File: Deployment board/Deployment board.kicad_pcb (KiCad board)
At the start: 2 copper layers, 50 x 50 mm, 27 parts, among them J1 Conn_01x04, J2 Conn_01x04, J3 Conn_01x02, J4 Conn_01x02, J5 Conn_01x02, M1 Motor_Servo, Q1 IRLR7843, Q2 IRLR7843, Q3 To be determined

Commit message: some changes on Deployment board pcb
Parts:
- C2: footprint Capacitor_THT:C_Radial_D10.0mm_H20.0mm_P5.00mm -> Capacitor_THT:C_Radial_D8.0mm_H7.0mm_P3.50mm
- moved D3 119.5 mm to (33.3, 150.1)
- moved R4 118.8 mm to (32.8, 147.1)
- moved GND1 118.7 mm to (37.0, 147.0)
- moved J3 113.1 mm to (27.4, 147.7)
- moved D6 108.6 mm to (39.0, 150.0)
- moved Q1 106.3 mm to (36.8, 141.6)
- moved V_D_BAT+1 105.9 mm to (39.5, 147.0)
- moved R7 105.7 mm to (43.2, 149.4), turned to 90 degrees
- moved R1 101.2 mm to (42.0, 136.0)
- moved D1 93.3 mm to (32.5, 136.0), turned to 180 degrees
- moved J1 92.7 mm to (27.4, 135.7)
- moved R6 90.0 mm to (37.0, 118.0)
- moved D5 81.1 mm to (42.5, 127.0), turned to 90 degrees
- moved R3 81.0 mm to (36.5, 136.0)
- moved F1 80.5 mm to (40.0, 119.0), turned to -90 degrees
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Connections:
- J3 pad 1: Net-(D3-A) -> V_Ｄ_BAT+
- J3 pad 2: unconnected-(J3-Pin_2-Pad2) -> Net-(D3-A)
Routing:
- net GND: track 0.00 -> 142.0 mm
- net V_Ｄ_BAT+: track 0.00 -> 52.8 mm
- net Net-(D3-A): track 0.00 -> 21.2 mm
- net Net-(D1-K): track 0.00 -> 19.3 mm
- net Main_AV_FIRE: track 0.00 -> 18.9 mm
- net Net-(D4-A): track 0.00 -> 16.0 mm
- net Backup_AV_FIRE: track 0.00 -> 13.1 mm
- net Backup_AV_PWM_Servo: track 0.00 -> 9.96 mm
- net Net-(D5-A2): track 0.00 -> 7.00 mm
- net V_D_BAT+: track 0.00 -> 4.25 mm
- net Main_AV_PWM_Servo: track 0.00 -> 4.22 mm
- net Net-(Q3-G): track 0.00 -> 3.49 mm
- net Net-(J5-Pin_1): track 0.00 -> 3.27 mm
- net Net-(D3-K): track 0.00 -> 3.01 mm
- net Net-(D6-A): track 0.00 -> 2.85 mm
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- added copper zone on B.Cu, net GND
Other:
- board size 50 x 50 mm -> 29.5 x 46.5 mm

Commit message: update Deployment board
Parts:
- J5: footprint Connector_PinHeader_2.54mm:PinHeader_1x02_P2.54mm_Vertical -> Connector_PinHeader_2.54mm:PinHeader_1x02_P2.54mm_Horizontal
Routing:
- net GND: track 142.0 -> 143.7 mm
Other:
- board size 29.5 x 46.5 mm -> 35.5 x 46.5 mm

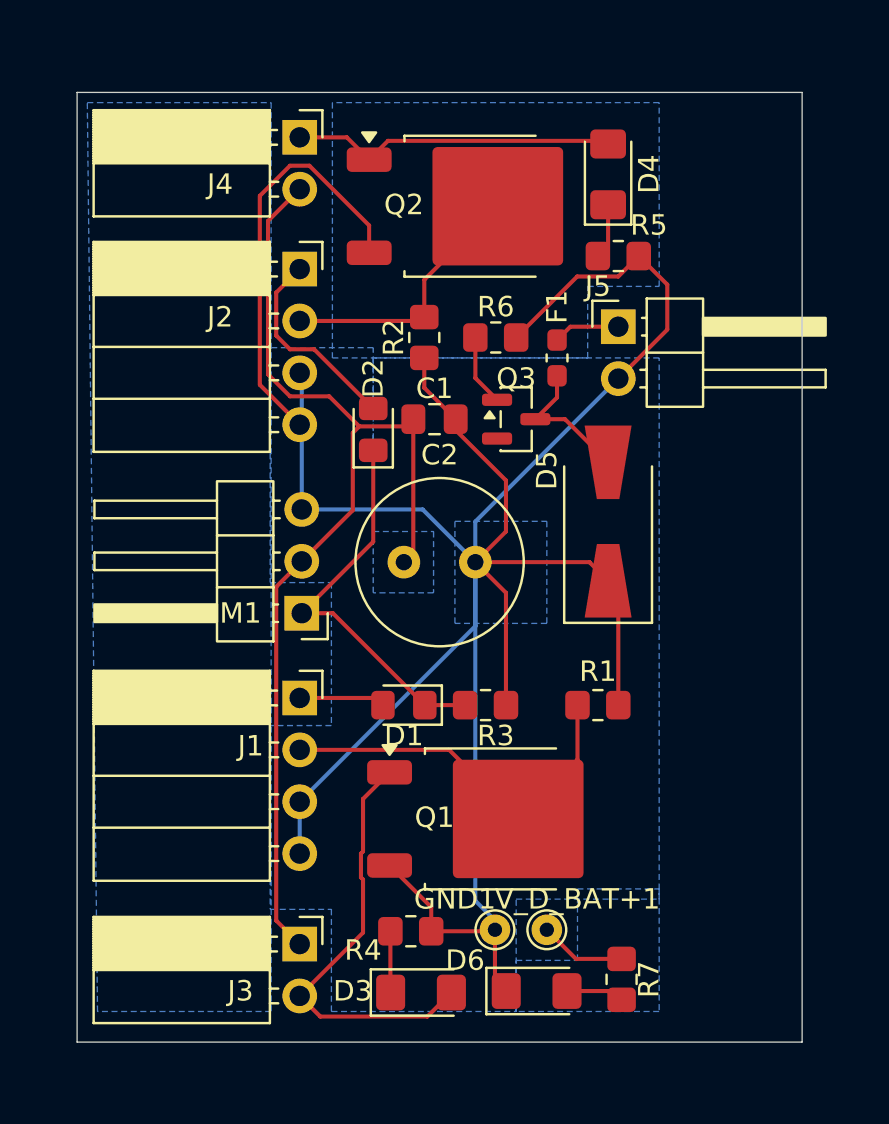
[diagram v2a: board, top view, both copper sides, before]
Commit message: add hole to connect wire
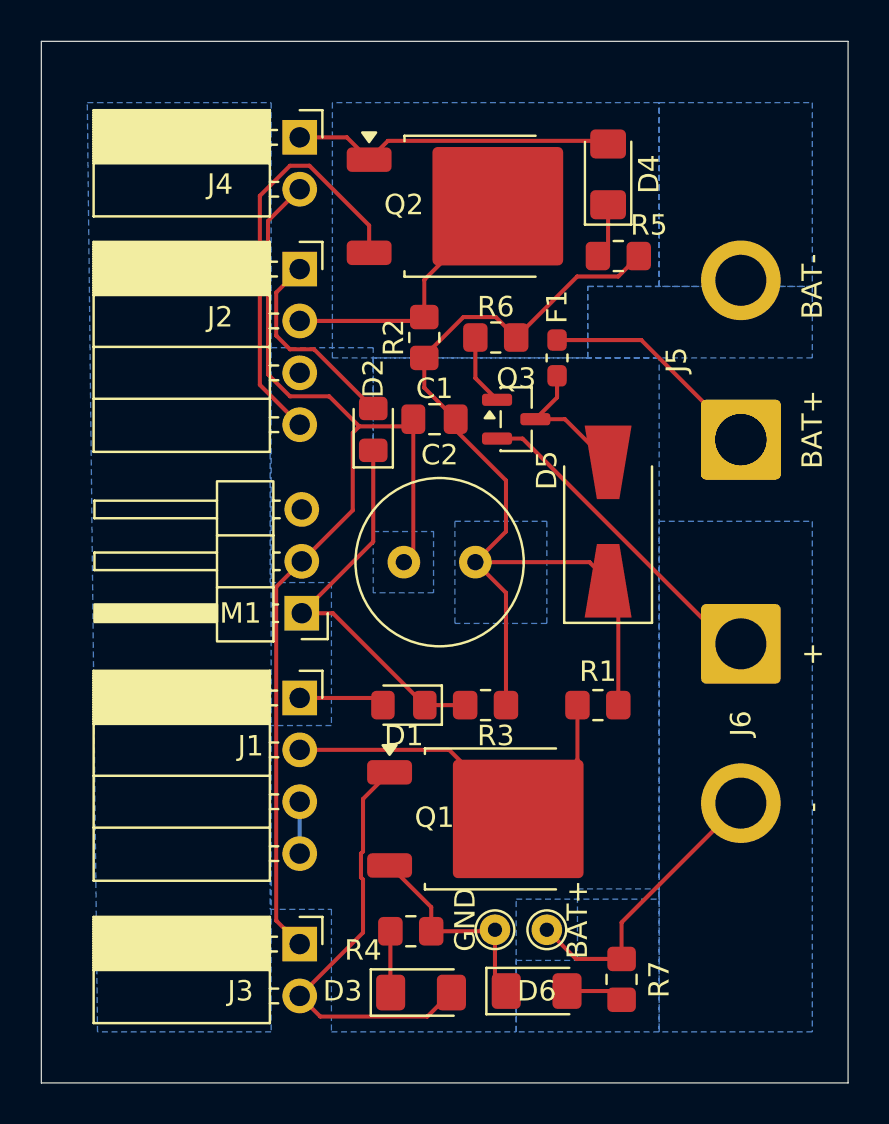
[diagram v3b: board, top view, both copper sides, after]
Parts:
- added ?: , , F.Cu at (49.0, 123.0)
- added J6: REMOVE BEFORE FLIGHT, Connector_Wire:SolderWire-2sqmm_1x02_P7.8mm_D2mm_OD3.9mm, F.Cu at (49.0, 133.0)
- J5: footprint Connector_PinHeader_2.54mm:PinHeader_1x02_P2.54mm_Horizontal -> Connector_Wire:SolderWire-2sqmm_1x02_P7.8mm_D2mm_OD3.9mm
- moved J5 8.16 mm to (49.0, 123.0), turned to 90 degrees
- renumbered V_D_BAT+1 to BAT+, GND1 to GND
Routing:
- net GND: track 143.7 -> 80.6 mm
- net Net-(J6-A): track 0.00 -> 16.1 mm
- net V_D_BAT+: track 4.25 -> 14.3 mm
- net Net-(J5-Pin_1): track 3.27 -> 11.0 mm
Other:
- board size 35.5 x 46.5 mm -> 39.5 x 51 mm
- board text added: "+"
- board text added: "-"
- board text added: "BAT+"
- board text added: "BAT-"

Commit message: jpush
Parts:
- removed ?: , 
- removed BAT+, GND: TestPoint, TestPoint:TestPoint_THTPad_D1.5mm_Drill0.7mm
- added GND1: TestPoint, TestPoint:TestPoint_THTPad_D1.5mm_Drill0.7mm, F.Cu at (40.5, 107.5)
- added V_D_BAT+1: TestPoint, TestPoint:TestPoint_THTPad_D1.5mm_Drill0.7mm, F.Cu at (35.5, 107.5)
- J1, J2: footprint Connector_PinSocket_2.54mm:PinSocket_1x04_P2.54mm_Horizontal -> Connector_PinSocket_2.54mm:PinSocket_1x04_P2.54mm_Vertical
- J3, J4: footprint Connector_PinSocket_2.54mm:PinSocket_1x02_P2.54mm_Horizontal -> Connector_PinSocket_2.54mm:PinSocket_1x02_P2.54mm_Vertical
- J5: footprint Connector_Wire:SolderWire-2sqmm_1x02_P7.8mm_D2mm_OD3.9mm -> Connector_JST:JST_EH_B2B-EH-A_1x02_P2.50mm_Vertical
- J6: footprint Connector_Wire:SolderWire-2sqmm_1x02_P7.8mm_D2mm_OD3.9mm -> Button_Switch_THT:SW_NKK_G1xJP
- M1: footprint Connector_PinHeader_2.54mm:PinHeader_1x03_P2.54mm_Horizontal -> Connector_PinHeader_2.54mm:PinHeader_1x03_P2.54mm_Vertical
- moved D6 44.4 mm to (26.0, 107.5)
- moved R7 43.5 mm to (31.5, 107.5), turned to 0 degrees
- moved J6 21.7 mm to (52.0, 111.5), turned to 180 degrees
- moved J3 18.6 mm to (43.5, 138.5)
- moved R4 18.3 mm to (49.0, 138.5)
- moved D3 18.3 mm to (49.5, 141.5), turned to 180 degrees
- moved D4 15.0 mm to (37.0, 124.0), turned to 0 degrees
- moved R5 14.9 mm to (32.0, 124.0), turned to -90 degrees
- moved J4 14.3 mm to (35.5, 120.0), turned to 90 degrees
- moved R3 14.2 mm to (29.0, 124.0), turned to 90 degrees
- moved Q3 10.0 mm to (46.0, 116.0), turned to 90 degrees
- moved J2 9.73 mm to (25.0, 124.1), turned to 180 degrees
- moved D5 9.61 mm to (51.0, 131.5)
- moved C1 8.52 mm to (42.5, 123.0)
- moved D2 8.47 mm to (25.0, 128.5), turned to 180 degrees
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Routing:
- net GND: track 80.6 -> 145.4 mm
- net V_Ｄ_BAT+: track 52.7 -> 31.5 mm
- net Net-(D3-A): track 21.2 -> 9.34 mm
- net V_D_BAT+: track 14.3 -> 3.00 mm
- net Net-(D5-A2): track 7.00 -> 16.3 mm
- net Main_AV_FIRE: track 18.9 -> 10.1 mm
- net Net-(J6-A): track 16.1 -> 7.51 mm
- net Net-(D1-K): track 19.3 -> 12.2 mm
- net Net-(J5-Pin_1): track 11.0 -> 4.81 mm
- net Backup_AV_PWM_Servo: track 9.96 -> 4.83 mm
- net Backup_AV_FIRE: track 13.1 -> 17.1 mm
- net Net-(D4-A): track 16.0 -> 12.8 mm
- net Net-(D4-K): track 2.72 -> 3.94 mm
- net Net-(D3-K): track 3.01 -> 4.21 mm
- net Main_AV_PWM_Servo: track 4.22 -> 5.02 mm
- removed copper zone on B.Cu, net GND
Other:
- board size 39.5 x 51 mm -> 35 x 45 mm
- board text removed: "+"
- board text removed: "-"
- board text removed: "BAT+"
- board text removed: "BAT-"
